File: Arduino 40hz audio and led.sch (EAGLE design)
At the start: 33 parts, among them IC1 LM7805, IC2 IRL-Z44N, IC3 LM741

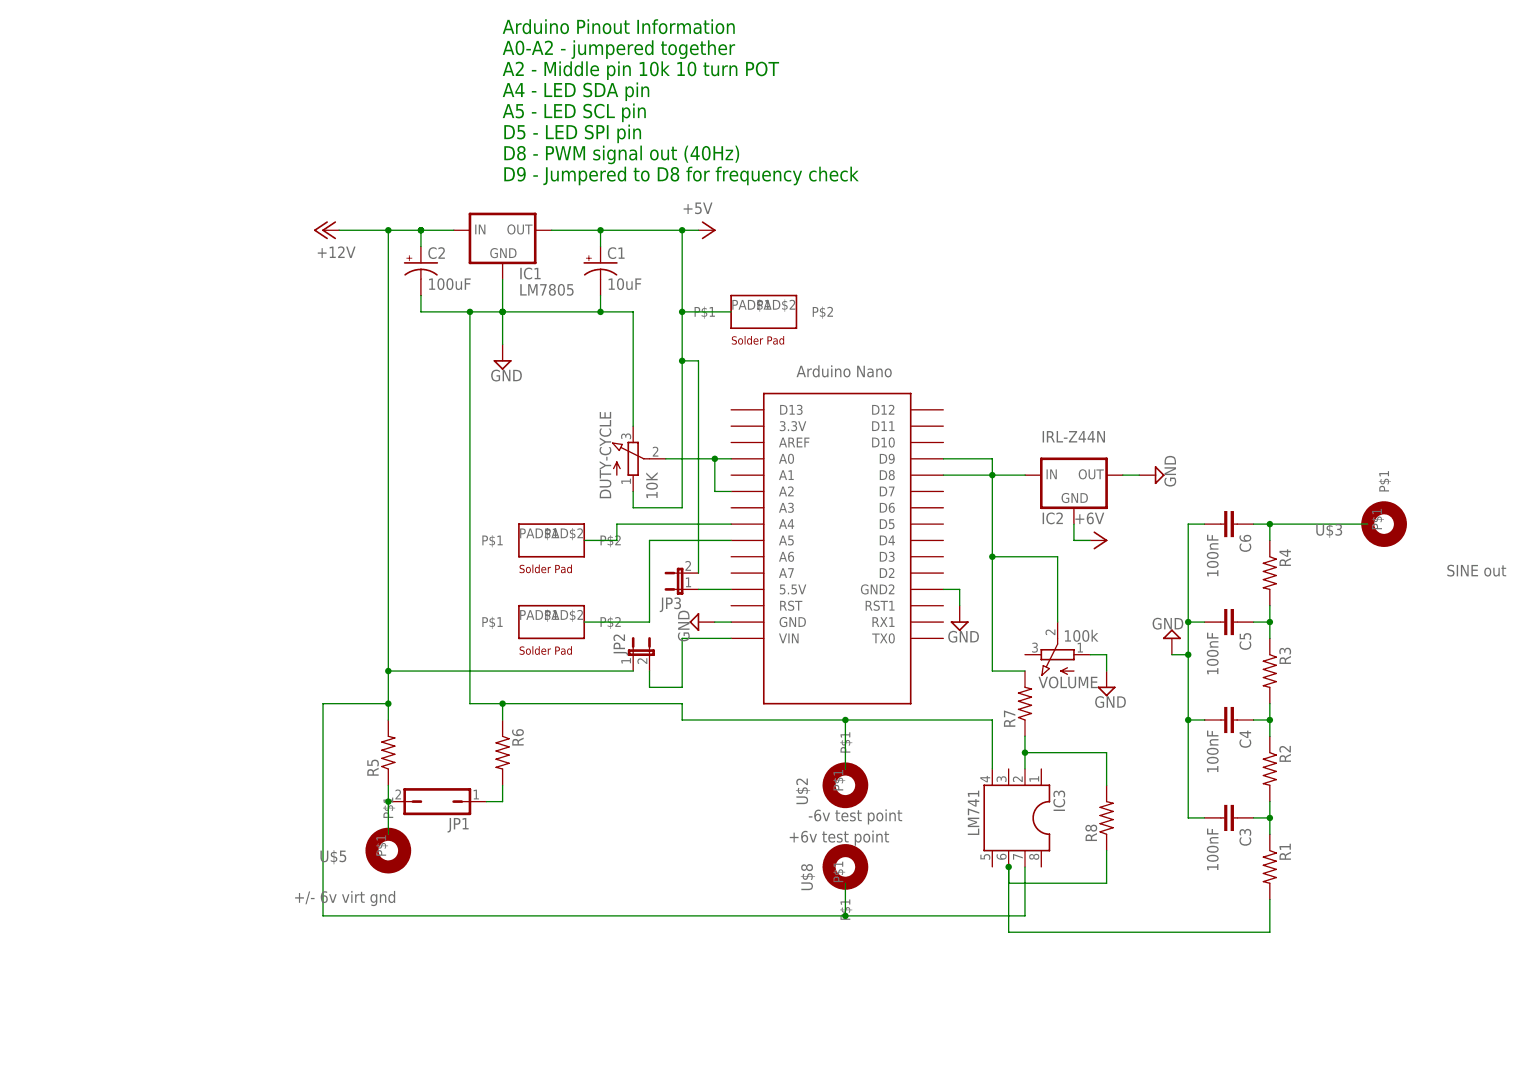
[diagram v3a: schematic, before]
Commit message: Tagging this v1.0.1
Tagging this v1.0.1.
* Fixed the +/- 6v traces and placement.
* Changed a few pads to be larger
* Added a pad for the LED out signal from D5
* Removed Jumper JP1
* Added drill holes, those this will vary until you have exact PCB board
sizes.
* Added dimention markers for where the drill holes are to make it easier
in Fusion360 for when I make the case
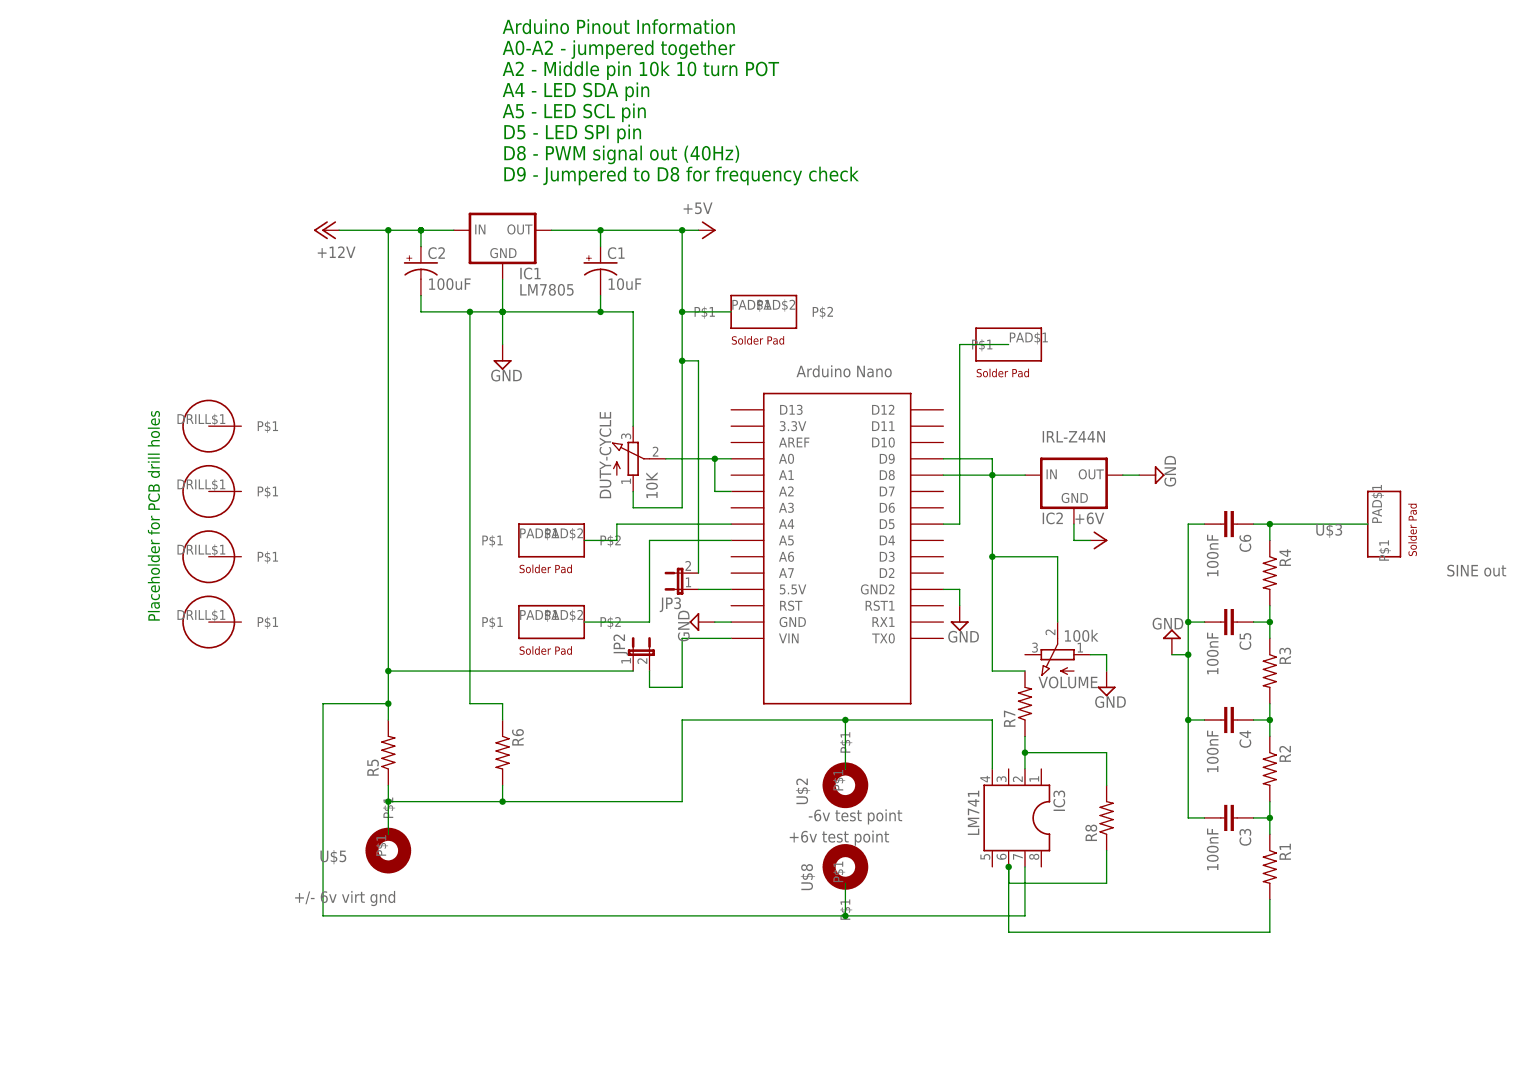
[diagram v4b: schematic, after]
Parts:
- removed JP1: (no value), jumper:JP1Q
- added U$10, U$11, U$12, U$13: DRILL-HOLE-4MM, jim_muppet_parts:DRILL-HOLE-4MM
- added U$9: PAD-1PIN-RECTANGLE, jim_muppet_parts:PAD-1PIN-RECTANGLE
- U$3: device jim_muppet_parts:PROBE-POINTPROBE_POINT_1 -> jim_muppet_parts:PAD-1PIN-RECTANGLE
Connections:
- removed net N$16: JP1.2, R5.1, U$5.P$1
- removed net N$7: JP1.1, R6.2
- new net N$11: U$1.D5, U$9.P$1
- new net N$12: IC3.4, R5.1, R6.2, U$2.P$1, U$5.P$1
- net GND: no longer IC3.4, U$2.P$1
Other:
- note added: "Placeholder for PCB drill holes"
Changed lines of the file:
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@@
 <part name="U$6" library="jim_muppet_parts" deviceset="PAD-2PIN-RECTANGLE" device=""/>
 <part name="U$7" library="jim_muppet_parts" deviceset="PAD-2PIN-RECTANGLE" device=""/>
-<part name="JP1" library="jumper" library_urn="urn:adsk.eagle:library:252" deviceset="JP1Q" device="" package3d_urn="urn:adsk.eagle:package:15455/1"/>
 <part name="U$5" library="jim_muppet_parts" deviceset="PROBE-POINT" device="PROBE_POINT_1" value="+/- 6v virt gnd"/>
 <part name="P+3" library="jim_muppet_parts" deviceset="+6V" device=""/>
@@
 <part name="JP3" library="jim_muppet_parts" deviceset="JUMPER-JP1E" device="" package3d_urn="urn:adsk.eagle:package:15455/1"/>
 <part name="R8" library="jim_muppet_parts" deviceset="RESISTOR" device="PTH-1/4W"/>
-<part name="U$3" library="jim_muppet_parts" deviceset="PROBE-POINT" device="PROBE_POINT_1" value="SINE out"/>
+<part name="U$3" library="jim_muppet_parts" deviceset="PAD-1PIN-RECTANGLE" device="" value="SINE out"/>
 <part name="U$2" library="jim_muppet_parts" deviceset="PROBE-POINT" device="PROBE_POINT_1" value="-6v test point"/>
 <part name="U$8" library="jim_muppet_parts" deviceset="PROBE-POINT" device="PROBE_POINT_1" value="+6v test point"/>
+<part name="U$9" library="jim_muppet_parts" deviceset="PAD-1PIN-RECTANGLE" device=""/>
+<part name="U$10" library="jim_muppet_parts" deviceset="DRILL-HOLE-4MM" device=""/>
+<part name="U$11" library="jim_muppet_parts" deviceset="DRILL-HOLE-4MM" device=""/>
+<part name="U$12" library="jim_muppet_parts" deviceset="DRILL-HOLE-4MM" device=""/>
+<part name="U$13" library="jim_muppet_parts" deviceset="DRILL-HOLE-4MM" device=""/>
 </parts>
 <sheets>
@@
 D9 - Jumpered to D8 for frequency check
 </text>
+<text x="-15.24" y="35.56" size="1.778" layer="91" rot="R90">Placeholder for PCB drill holes</text>
 </plain>
 <instances>
@@
 <instance part="U$6" gate="G$1" x="45.72" y="35.56" smashed="yes"/>
 <instance part="U$7" gate="G$1" x="78.74" y="83.82" smashed="yes"/>
-<instance part="JP1" gate="A" x="27.94" y="7.62" smashed="yes" rot="R90">
-<attribute name="NAME" x="33.02" y="5.08" size="1.778" layer="95" rot="R180"/>
-<attribute name="VALUE" x="33.02" y="12.065" size="1.778" layer="96" rot="R180"/>
-</instance>
 <instance part="U$5" gate="G$1" x="20.32" y="0" smashed="yes" rot="R90">
 <attribute name="NAME" x="13.97" y="0" size="1.778" layer="95" rot="R180"/>
@@
 <attribute name="VALUE" x="82.55" y="1.27" size="1.778" layer="96"/>
 </instance>
+<instance part="U$9" gate="G$1" x="116.84" y="78.74" smashed="yes"/>
+<instance part="U$10" gate="G$1" x="-7.62" y="66.04" smashed="yes"/>
+<instance part="U$11" gate="G$1" x="-7.62" y="55.88" smashed="yes"/>
+<instance part="U$12" gate="G$1" x="-7.62" y="45.72" smashed="yes"/>
+<instance part="U$13" gate="G$1" x="-7.62" y="35.56" smashed="yes"/>
 </instances>
 <busses>
@@
 <wire x1="58.42" y1="83.82" x2="53.34" y2="83.82" width="0.1524" layer="91"/>
 <junction x="53.34" y="83.82"/>
-<wire x1="38.1" y1="20.32" x2="38.1" y2="22.86" width="0.1524" layer="91"/>
 <junction x="33.02" y="83.82"/>
-<pinref part="R6" gate="G$1" pin="1"/>
 <wire x1="33.02" y1="22.86" x2="33.02" y2="83.82" width="0.1524" layer="91"/>
 <wire x1="33.02" y1="22.86" x2="38.1" y2="22.86" width="0.1524" layer="91"/>
-<wire x1="38.1" y1="22.86" x2="66.04" y2="22.86" width="0.1524" layer="91"/>
-<junction x="38.1" y="22.86"/>
-<wire x1="66.04" y1="22.86" x2="66.04" y2="20.32" width="0.1524" layer="91"/>
-<pinref part="IC3" gate="G$1" pin="4"/>
-<wire x1="114.3" y1="20.32" x2="114.3" y2="12.7" width="0.1524" layer="91"/>
-<wire x1="91.44" y1="20.32" x2="114.3" y2="20.32" width="0.1524" layer="91"/>
-<pinref part="U$2" gate="G$1" pin="P$1"/>
-<wire x1="91.44" y1="12.7" x2="91.44" y2="20.32" width="0.1524" layer="91"/>
-<wire x1="66.04" y1="20.32" x2="91.44" y2="20.32" width="0.1524" layer="91"/>
-<junction x="91.44" y="20.32"/>
+<pinref part="R6" gate="G$1" pin="1"/>
+<wire x1="38.1" y1="20.32" x2="38.1" y2="22.86" width="0.1524" layer="91"/>
 </segment>
 <segment>
@@
 </segment>
 </net>
-<net name="N$16" class="0">
-<segment>
-<wire x1="20.32" y1="10.16" x2="20.32" y2="7.62" width="0.1524" layer="91"/>
-<pinref part="JP1" gate="A" pin="2"/>
-<pinref part="U$5" gate="G$1" pin="P$1"/>
-<wire x1="20.32" y1="7.62" x2="20.32" y2="2.54" width="0.1524" layer="91"/>
-<junction x="20.32" y="7.62"/>
-<pinref part="R5" gate="G$1" pin="1"/>
-</segment>
-</net>
-<net name="N$7" class="0">
-<segment>
-<pinref part="JP1" gate="A" pin="1"/>
-<pinref part="R6" gate="G$1" pin="2"/>
-<wire x1="35.56" y1="7.62" x2="38.1" y2="7.62" width="0.1524" layer="91"/>
-<wire x1="38.1" y1="7.62" x2="38.1" y2="10.16" width="0.1524" layer="91"/>
-</segment>
-</net>
 <net name="N$6" class="0">
 <segment>
@@
 </segment>
 </net>
+<net name="N$11" class="0">
+<segment>
+<pinref part="U$9" gate="G$1" pin="P$1"/>
+<wire x1="116.84" y1="78.74" x2="109.22" y2="78.74" width="0.1524" layer="91"/>
+<wire x1="109.22" y1="78.74" x2="109.22" y2="50.8" width="0.1524" layer="91"/>
+<pinref part="U$1" gate="G$1" pin="D5"/>
+<wire x1="109.22" y1="50.8" x2="106.68" y2="50.8" width="0.1524" layer="91"/>
+</segment>
+</net>
+<net name="N$12" class="0">
+<segment>
+<pinref part="R6" gate="G$1" pin="2"/>
+<wire x1="38.1" y1="7.62" x2="38.1" y2="10.16" width="0.1524" layer="91"/>
+<pinref part="U$5" gate="G$1" pin="P$1"/>
+<pinref part="R5" gate="G$1" pin="1"/>
+<wire x1="20.32" y1="10.16" x2="20.32" y2="7.62" width="0.1524" layer="91"/>
+<wire x1="20.32" y1="7.62" x2="20.32" y2="2.54" width="0.1524" layer="91"/>
+<wire x1="38.1" y1="7.62" x2="20.32" y2="7.62" width="0.1524" layer="91"/>
+<junction x="38.1" y="7.62"/>
+<junction x="20.32" y="7.62"/>
+<pinref part="IC3" gate="G$1" pin="4"/>
+<wire x1="114.3" y1="20.32" x2="114.3" y2="12.7" width="0.1524" layer="91"/>
+<wire x1="91.44" y1="20.32" x2="114.3" y2="20.32" width="0.1524" layer="91"/>
+<pinref part="U$2" gate="G$1" pin="P$1"/>
+<wire x1="91.44" y1="12.7" x2="91.44" y2="20.32" width="0.1524" layer="91"/>
+<wire x1="66.04" y1="7.62" x2="66.04" y2="20.32" width="0.1524" layer="91"/>
+<wire x1="66.04" y1="20.32" x2="91.44" y2="20.32" width="0.1524" layer="91"/>
+<junction x="91.44" y="20.32"/>
+<wire x1="38.1" y1="7.62" x2="66.04" y2="7.62" width="0.1524" layer="91"/>
+</segment>
+</net>

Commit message: This will be the final version of design
This will be the final version of design unless I come up with something
more amazing.  At this point I will just be making minor tweaks.

The next phase of this effort will be to go from sine to square via a
Schmitt trigger.
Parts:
- added U$14: PAD-1PIN-RECTANGLE175, jim_muppet_parts:PAD-1PIN-RECTANGLE175
- R1, R2, R3, R4: value (none) -> 39k
- R5, R6: value (none) -> 1k
- R7: value (none) -> 600R
- R8: value (none) -> 4k
- U$3: device jim_muppet_parts:PAD-1PIN-RECTANGLE -> jim_muppet_parts:PAD-1PIN-RECTANGLE200
- U$4: value PAD-2PIN-RECTANGLE -> SCL; device jim_muppet_parts:PAD-2PIN-RECTANGLE -> jim_muppet_parts:PAD-1PIN-RECTANGLE175
- U$6: value PAD-2PIN-RECTANGLE -> PAD-1PIN-RECTANGLE175; device jim_muppet_parts:PAD-2PIN-RECTANGLE -> jim_muppet_parts:PAD-1PIN-RECTANGLE175
- U$9: value PAD-1PIN-RECTANGLE -> PAD-1PIN-RECTANGLE175; device jim_muppet_parts:PAD-1PIN-RECTANGLE -> jim_muppet_parts:PAD-1PIN-RECTANGLE175
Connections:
- net N$14: no longer U$4.P$2
- net N$15: no longer U$6.P$2
- net N$2: now also U$14.P$1
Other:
- note added: "LCD SCL"
- note added: "LCD SDA"
